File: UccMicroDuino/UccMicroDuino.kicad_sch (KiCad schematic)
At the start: 8 parts, among them J2 Conn_01x10_Socket, J2 USB_A, U2 ATtiny85-20S

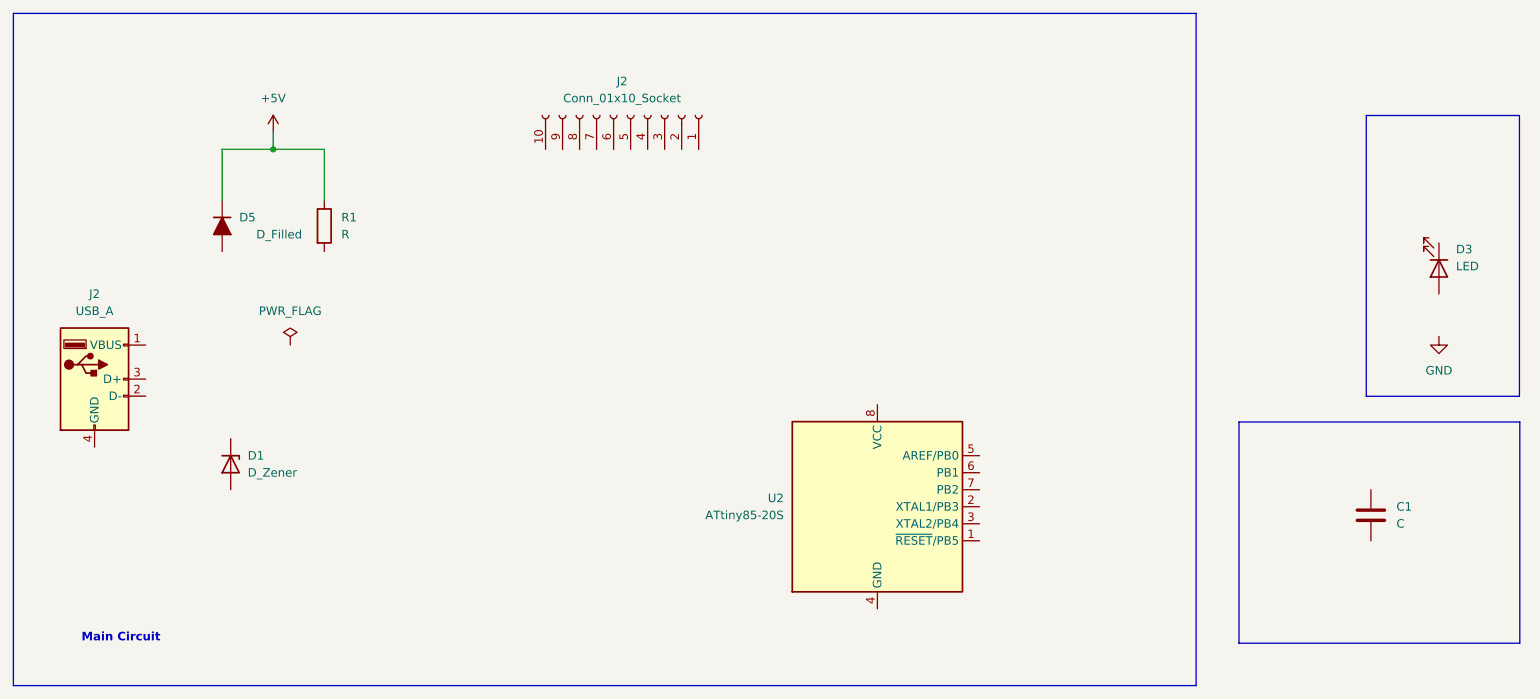
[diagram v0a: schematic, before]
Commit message: Esquematico principal completo con Power Led y DC Power
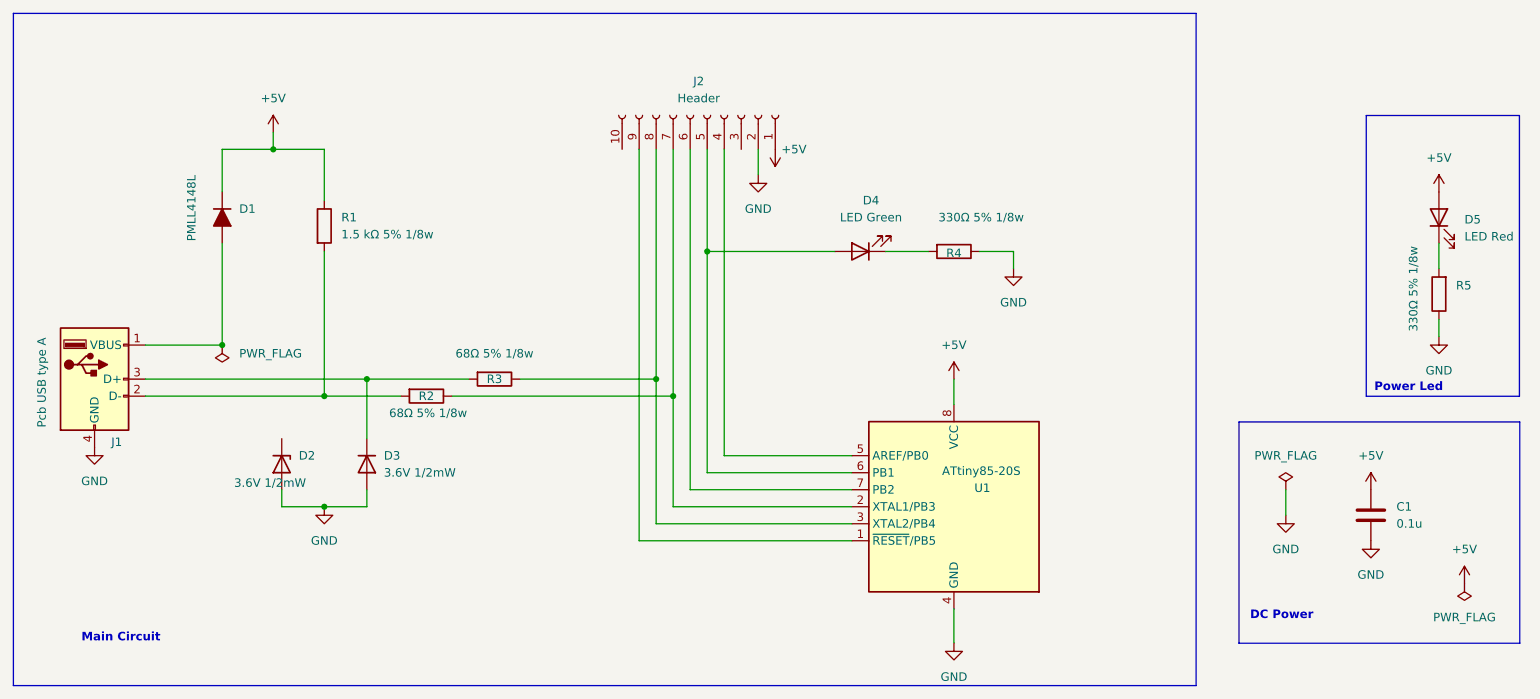
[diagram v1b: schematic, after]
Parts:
- added D3: 3.6V 1/2mW, symbol Device:D
- added D4: LED Green, symbol Device:LED
- added R2, R3: 68Ω 5% 1/8w, symbol Device:R
- added R4, R5: 330Ω 5% 1/8w, symbol Device:R
- C1: value C -> 0.1u
- D1: renamed from D5; value D_Filled -> PMLL4148L
- D2: renamed from D1; value D_Zener -> 3.6V 1/2mW
- D5: renamed from D3; value LED -> LED Red
- J1: renamed from J2; value USB_A -> Pcb USB type A
- J2: value Conn_01x10_Socket -> Header
- R1: value R -> 1.5 kΩ 5% 1/8w
- renumbered U2 to U1
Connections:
- net +5V: now also C1.1, D5.2 (A), J2.1 (Pin_1), U1.8 (VCC)
- net GND: now also C1.2, D2.2 (A), J1.4 (GND), J2.2 (Pin_2), U1.4 (GND), D3.2 (A), R4.1, R5.1
- net at D5.1 (K): now also R5.2
- net at R1.2: now also J1.2 (D-), R2.2
- net at U1.1 (~{RESET}/PB5): now also J2.9 (Pin_9)
- net at U1.2 (XTAL1/PB3): now also J2.7 (Pin_7), R2.1
- net at U1.3 (XTAL2/PB4): now also J2.8 (Pin_8), R3.1
- net at U1.5 (AREF/PB0): now also J2.4 (Pin_4)
- net at U1.6 (PB1): now also J2.5 (Pin_5), D4.2 (A)
- net at U1.7 (PB2): now also J2.6 (Pin_6)
- net at J1.1 (VBUS): now also D1.2 (A)
- net at J1.3 (D+): now also D3.1 (K), R3.2
- new net: D4.1 (K), R4.2
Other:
- note added: "DC Power"
- note added: "Power Led"
- moved on the sheet: D1, D2, D5, J2, U1
